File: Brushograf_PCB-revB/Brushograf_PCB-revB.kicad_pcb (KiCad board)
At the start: 2 copper layers, 200 x 60 mm, 76 parts, among them J1 Conn_01x05_Socket, J12 USB-C PD in, J13 Pendant, J2 Conn_01x05_Socket, J3 Conn_01x05_Socket, J8 SD_CARD_MICRO_AMPHENOL_114008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, SW1 ESP POWER, SW2 SW_Lever_1P2T_NKK_GW12LxH, U1 ULN2003A, U2 ULN2003A, U3 ULN2003A, U4 ESP32-DevKitC, U6 CH224K, U7 TPS54202, U8 TPS54202

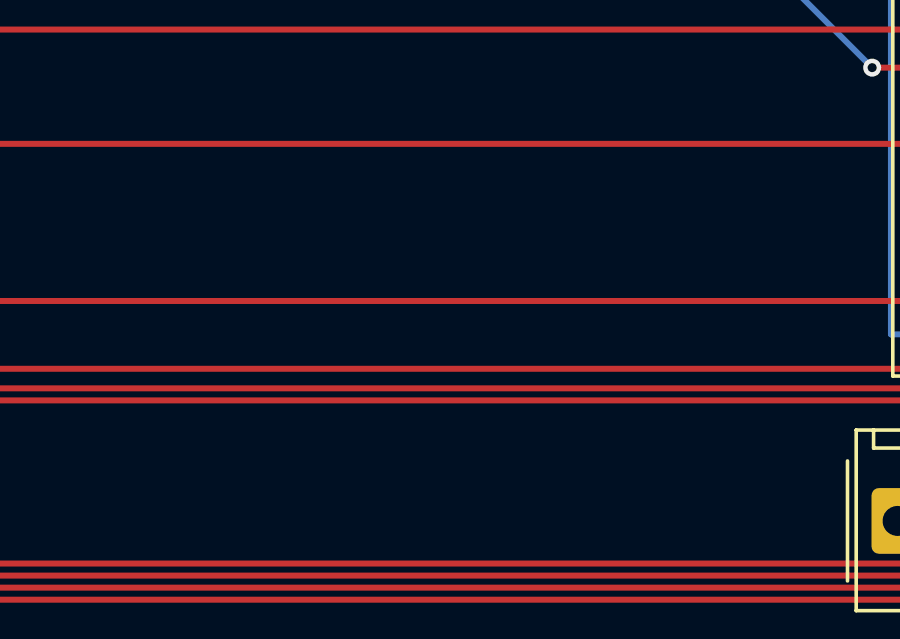
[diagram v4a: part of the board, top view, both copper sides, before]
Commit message: Move J7 to Y=50 and swap GND/PROBE pinout
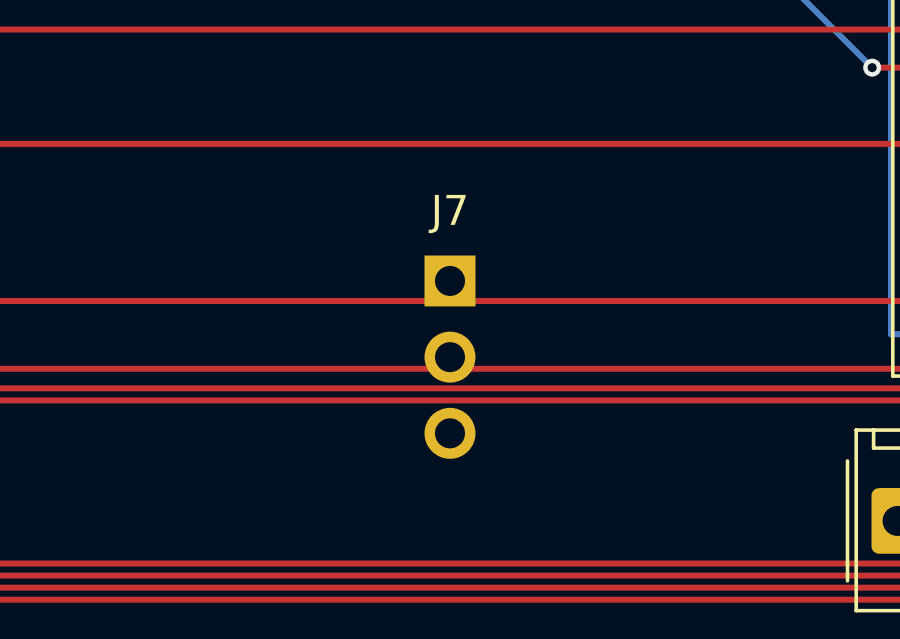
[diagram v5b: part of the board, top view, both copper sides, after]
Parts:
- added J7: Conn_01x03_Pin, Connector_PinHeader_2.54mm:PinHeader_1x03_P2.54mm_Vertical, F.Cu at (110.0, 50.0)
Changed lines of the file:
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@@
 		)
 		(embedded_fonts no)
-		(model "${KICAD8_3DMODEL_DIR}/LED_THT.3dshapes/LED_D1.8mm_W3.3mm_H2.4mm.wrl"
+		(model "${KICAD10_3DMODEL_DIR}/LED_THT.3dshapes/LED_D1.8mm_W3.3mm_H2.4mm.step"
 			(offset
 				(xyz 0 0 0)
@@
 		)
 		(embedded_fonts no)
-		(model "${KICAD8_3DMODEL_DIR}/LED_THT.3dshapes/LED_D1.8mm_W3.3mm_H2.4mm.wrl"
+		(model "${KICAD10_3DMODEL_DIR}/LED_THT.3dshapes/LED_D1.8mm_W3.3mm_H2.4mm.step"
 			(offset
 				(xyz 0 0 0)
@@
 		)
 		(embedded_fonts no)
-		(model "${KICAD8_3DMODEL_DIR}/Connector_Molex.3dshapes/Molex_KK-254_AE-6410-05A_1x05_P2.54mm_Vertical.wrl"
+		(model "${KICAD10_3DMODEL_DIR}/Connector_Molex.3dshapes/Molex_KK-254_AE-6410-05A_1x05_P2.54mm_Vertical.step"
 			(offset
 				(xyz 0 0 0)
@@
 		)
 		(embedded_fonts no)
-		(model "${KICAD8_3DMODEL_DIR}/LED_THT.3dshapes/LED_D1.8mm_W3.3mm_H2.4mm.wrl"
+		(model "${KICAD10_3DMODEL_DIR}/LED_THT.3dshapes/LED_D1.8mm_W3.3mm_H2.4mm.step"
 			(offset
 				(xyz 0 0 0)
@@
 		)
 		(embedded_fonts no)
-		(model "${KICAD8_3DMODEL_DIR}/Package_DIP.3dshapes/DIP-16_W7.62mm_Socket.wrl"
+		(model "${KICAD10_3DMODEL_DIR}/Package_DIP.3dshapes/DIP-16_W7.62mm_Socket.step"
 			(offset
 				(xyz 0 0 0)
@@
 		)
 		(embedded_fonts no)
-		(model "${KICAD8_3DMODEL_DIR}/LED_THT.3dshapes/LED_D1.8mm_W3.3mm_H2.4mm.wrl"
+		(model "${KICAD10_3DMODEL_DIR}/LED_THT.3dshapes/LED_D1.8mm_W3.3mm_H2.4mm.step"
 			(offset
 				(xyz 0 0 0)
@@
 		)
 		(embedded_fonts no)
-		(model "${KICAD8_3DMODEL_DIR}/LED_THT.3dshapes/LED_D1.8mm_W3.3mm_H2.4mm.wrl"
+		(model "${KICAD10_3DMODEL_DIR}/LED_THT.3dshapes/LED_D1.8mm_W3.3mm_H2.4mm.step"
 			(offset
 				(xyz 0 0 0)
@@
 		)
 		(embedded_fonts no)
-		(model "${KICAD8_3DMODEL_DIR}/LED_THT.3dshapes/LED_D1.8mm_W3.3mm_H2.4mm.wrl"
+		(model "${KICAD10_3DMODEL_DIR}/LED_THT.3dshapes/LED_D1.8mm_W3.3mm_H2.4mm.step"
 			(offset
 				(xyz 0 0 0)
@@
 		)
 		(embedded_fonts no)
-		(model "${KICAD8_3DMODEL_DIR}/LED_THT.3dshapes/LED_D1.8mm_W3.3mm_H2.4mm.wrl"
+		(model "${KICAD10_3DMODEL_DIR}/LED_THT.3dshapes/LED_D1.8mm_W3.3mm_H2.4mm.step"
 			(offset
 				(xyz 0 0 0)
@@
 		)
 		(embedded_fonts no)
-		(model "${KICAD8_3DMODEL_DIR}/LED_THT.3dshapes/LED_D1.8mm_W3.3mm_H2.4mm.wrl"
+		(model "${KICAD10_3DMODEL_DIR}/LED_THT.3dshapes/LED_D1.8mm_W3.3mm_H2.4mm.step"
 			(offset
 				(xyz 0 0 0)
@@
 		)
 		(embedded_fonts no)
-		(model "${KICAD8_3DMODEL_DIR}/Package_DIP.3dshapes/DIP-16_W7.62mm_Socket.wrl"
+		(model "${KICAD10_3DMODEL_DIR}/Package_DIP.3dshapes/DIP-16_W7.62mm_Socket.step"
 			(offset
 				(xyz 0 0 0)
@@
 		)
 		(embedded_fonts no)
-		(model "${KICAD8_3DMODEL_DIR}/LED_THT.3dshapes/LED_D1.8mm_W3.3mm_H2.4mm.wrl"
+		(model "${KICAD10_3DMODEL_DIR}/LED_THT.3dshapes/LED_D1.8mm_W3.3mm_H2.4mm.step"
 			(offset
 				(xyz 0 0 0)
@@
 		)
 		(embedded_fonts no)
-		(model "${KICAD8_3DMODEL_DIR}/Connector_Molex.3dshapes/Molex_KK-254_AE-6410-05A_1x05_P2.54mm_Vertical.wrl"
+		(model "${KICAD10_3DMODEL_DIR}/Connector_Molex.3dshapes/Molex_KK-254_AE-6410-05A_1x05_P2.54mm_Vertical.step"
 			(offset
 				(xyz 0 0 0)
@@
 		)
 		(embedded_fonts no)
-		(model "${KICAD8_3DMODEL_DIR}/LED_THT.3dshapes/LED_D1.8mm_W3.3mm_H2.4mm.wrl"
+		(model "${KICAD10_3DMODEL_DIR}/LED_THT.3dshapes/LED_D1.8mm_W3.3mm_H2.4mm.step"
 			(offset
 				(xyz 0 0 0)
@@
 		)
 		(embedded_fonts no)
-		(model "${KICAD8_3DMODEL_DIR}/Connector_Molex.3dshapes/Molex_KK-254_AE-6410-05A_1x05_P2.54mm_Vertical.wrl"
+		(model "${KICAD10_3DMODEL_DIR}/Connector_Molex.3dshapes/Molex_KK-254_AE-6410-05A_1x05_P2.54mm_Vertical.step"
 			(offset
 				(xyz 0 0 0)
@@
 		)
 		(embedded_fonts no)
-		(model "${KICAD8_3DMODEL_DIR}/LED_THT.3dshapes/LED_D1.8mm_W3.3mm_H2.4mm.wrl"
+		(model "${KICAD10_3DMODEL_DIR}/LED_THT.3dshapes/LED_D1.8mm_W3.3mm_H2.4mm.step"
 			(offset
 				(xyz 0 0 0)
@@
 		)
 		(embedded_fonts no)
-		(model "${KICAD8_3DMODEL_DIR}/Package_DIP.3dshapes/DIP-16_W7.62mm_Socket.wrl"
+		(model "${KICAD10_3DMODEL_DIR}/Package_DIP.3dshapes/DIP-16_W7.62mm_Socket.step"
 			(offset
 				(xyz 0 0 0)
@@
 		)
 		(embedded_fonts no)
-		(model "${KICAD8_3DMODEL_DIR}/LED_THT.3dshapes/LED_D1.8mm_W3.3mm_H2.4mm.wrl"
+		(model "${KICAD10_3DMODEL_DIR}/LED_THT.3dshapes/LED_D1.8mm_W3.3mm_H2.4mm.step"
 			(offset
 				(xyz 0 0 0)
@@
 		)
 		(embedded_fonts no)
-		(model "${KISYS3DMOD}/Resistor_SMD.3dshapes/R_1206_3216Metric.wrl"
+		(model "${KICAD10_3DMODEL_DIR}/Resistor_SMD.3dshapes/R_1206_3216Metric.step"
 			(offset
 				(xyz 0 0 0)
@@
 		)
 		(embedded_fonts no)
-		(model "${KISYS3DMOD}/Resistor_SMD.3dshapes/R_1206_3216Metric.wrl"
+		(model "${KICAD10_3DMODEL_DIR}/Resistor_SMD.3dshapes/R_1206_3216Metric.step"
 			(offset
 				(xyz 0 0 0)
@@
 		)
 		(embedded_fonts no)
-		(model "${KISYS3DMOD}/Resistor_SMD.3dshapes/R_1206_3216Metric.wrl"
+		(model "${KICAD10_3DMODEL_DIR}/Resistor_SMD.3dshapes/R_1206_3216Metric.step"
 			(offset
 				(xyz 0 0 0)
@@
 		)
 		(embedded_fonts no)
-		(model "${KISYS3DMOD}/Resistor_SMD.3dshapes/R_1206_3216Metric.wrl"
+		(model "${KICAD10_3DMODEL_DIR}/Resistor_SMD.3dshapes/R_1206_3216Metric.step"
 			(offset
 				(xyz 0 0 0)
@@
 		)
 		(embedded_fonts no)
-		(model "${KICAD6_3DMODEL_DIR}/Capacitor_SMD.3dshapes/C_1206_3216Metric.wrl"
+		(model "${KICAD10_3DMODEL_DIR}/Capacitor_SMD.3dshapes/C_1206_3216Metric.step"
 			(offset
 				(xyz 0 0 0)
@@
 		)
 		(embedded_fonts no)
-		(model "${KICAD6_3DMODEL_DIR}/Capacitor_SMD.3dshapes/C_1206_3216Metric.wrl"
+		(model "${KICAD10_3DMODEL_DIR}/Capacitor_SMD.3dshapes/C_1206_3216Metric.step"
 			(offset
 				(xyz 0 0 0)
@@
 		)
 		(embedded_fonts no)
-		(model "${KISYS3DMOD}/Resistor_SMD.3dshapes/R_1206_3216Metric.wrl"
+		(model "${KICAD10_3DMODEL_DIR}/Resistor_SMD.3dshapes/R_1206_3216Metric.step"
 			(offset
 				(xyz 0 0 0)
@@
 		)
 		(embedded_fonts no)
-		(model "${KISYS3DMOD}/Resistor_SMD.3dshapes/R_1206_3216Metric.wrl"
+		(model "${KICAD10_3DMODEL_DIR}/Resistor_SMD.3dshapes/R_1206_3216Metric.step"
 			(offset
 				(xyz 0 0 0)
@@
 		)
 		(embedded_fonts no)
-		(model "${KISYS3DMOD}/Resistor_SMD.3dshapes/R_1206_3216Metric.wrl"
+		(model "${KICAD10_3DMODEL_DIR}/Resistor_SMD.3dshapes/R_1206_3216Metric.step"
 			(offset
 				(xyz 0 0 0)
@@
 		)
 		(embedded_fonts no)
-		(model "${KISYS3DMOD}/Resistor_SMD.3dshapes/R_1206_3216Metric.wrl"
+		(model "${KICAD10_3DMODEL_DIR}/Resistor_SMD.3dshapes/R_1206_3216Metric.step"
 			(offset
 				(xyz 0 0 0)
@@
 		)
 		(embedded_fonts no)
-		(model "${KISYS3DMOD}/Resistor_SMD.3dshapes/R_1206_3216Metric.wrl"
+		(model "${KICAD10_3DMODEL_DIR}/Resistor_SMD.3dshapes/R_1206_3216Metric.step"
 			(offset
 				(xyz 0 0 0)
@@
 		)
 		(embedded_fonts no)
-		(model "${KISYS3DMOD}/Resistor_SMD.3dshapes/R_1206_3216Metric.wrl"
+		(model "${KICAD10_3DMODEL_DIR}/Resistor_SMD.3dshapes/R_1206_3216Metric.step"
 			(offset
 				(xyz 0 0 0)
@@
 		)
 		(embedded_fonts no)
-		(model "${KISYS3DMOD}/Resistor_SMD.3dshapes/R_1206_3216Metric.wrl"
+		(model "${KICAD10_3DMODEL_DIR}/Resistor_SMD.3dshapes/R_1206_3216Metric.step"
 			(offset
 				(xyz 0 0 0)
@@
 		)
 		(embedded_fonts no)
-		(model "${KISYS3DMOD}/Resistor_SMD.3dshapes/R_1206_3216Metric.wrl"
+		(model "${KICAD10_3DMODEL_DIR}/Resistor_SMD.3dshapes/R_1206_3216Metric.step"
 			(offset
 				(xyz 0 0 0)
@@
 		)
 		(embedded_fonts no)
-		(model "${KICAD6_3DMODEL_DIR}/Capacitor_SMD.3dshapes/C_1206_3216Metric.wrl"
+		(model "${KICAD10_3DMODEL_DIR}/Capacitor_SMD.3dshapes/C_1206_3216Metric.step"
 			(offset
 				(xyz 0 0 0)
@@
 	)
 	(embedded_fonts no)
+	(footprint "Connector_PinHeader_2.54mm:PinHeader_1x03_P2.54mm_Vertical"
+		(layer "F.Cu")
+		(at 110 50)
+		(property "Reference" "J7"
+			(at 0 -2.33 0)
+			(layer "F.SilkS")
+			(effects
+				(font
+					(size 1 1)
+					(thickness 0.15)
+				)
+			)
+		)
+		(property "Value" "Conn_01x03_Pin"
+			(at 0 7.41 0)
+			(layer "F.Fab")
+			(effects
+				(font
+					(size 1 1)
+					(thickness 0.15)
+				)
+			)
+		)
+		(pad "1" thru_hole rect
+			(at 0 0)
+			(size 1.7 1.7)
+			(drill 1)
+			(layers "*.Cu" "*.Mask")
+			(remove_unused_layers no)
+			(net "3.3V")
+		)
+		(pad "2" thru_hole oval
+			(at 0 2.54)
+			(size 1.7 1.7)
+			(drill 1)
+			(layers "*.Cu" "*.Mask")
+			(remove_unused_layers no)
+			(net "GND")
+		)
+		(pad "3" thru_hole oval
+			(at 0 5.08)
+			(size 1.7 1.7)
+			(drill 1)
+			(layers "*.Cu" "*.Mask")
+			(remove_unused_layers no)
+			(net "PROBE")
+		)
+	)
 )

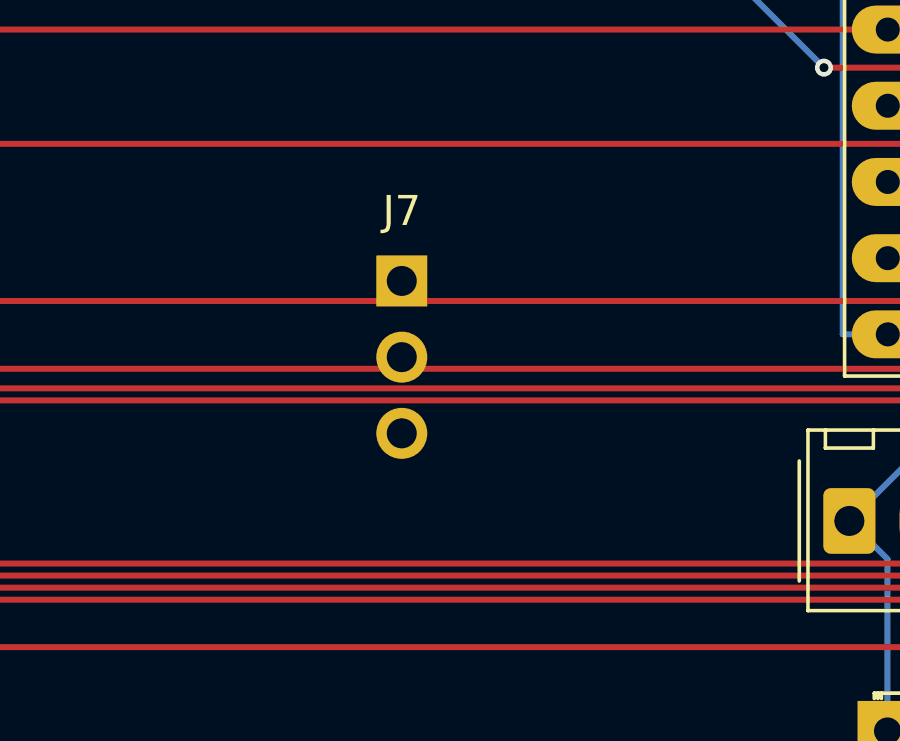
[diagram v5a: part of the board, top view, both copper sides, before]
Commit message: Change J7 to horizontal header at Y=58 and rotate 90 deg
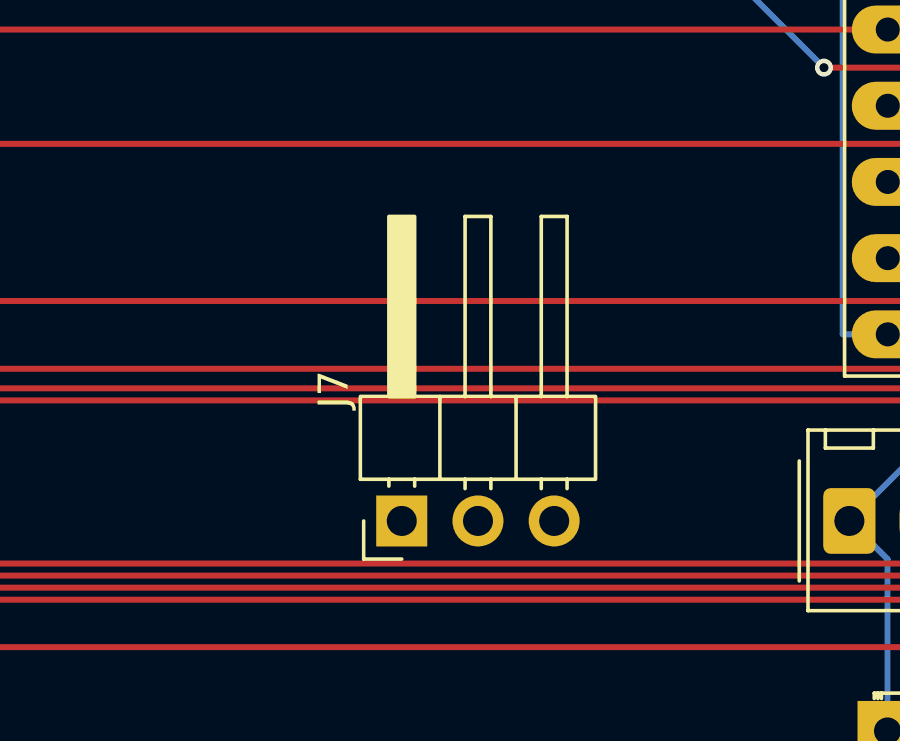
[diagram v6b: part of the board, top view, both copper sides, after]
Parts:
- J7: value Conn_01x03_Pin -> PinHeader_1x03_P2.54mm_Horizontal; footprint Connector_PinHeader_2.54mm:PinHeader_1x03_P2.54mm_Vertical -> PinHeader_1x03_P2.54mm_Horizontal
- moved J7 8.00 mm to (110.0, 58.0), turned to 90 degrees

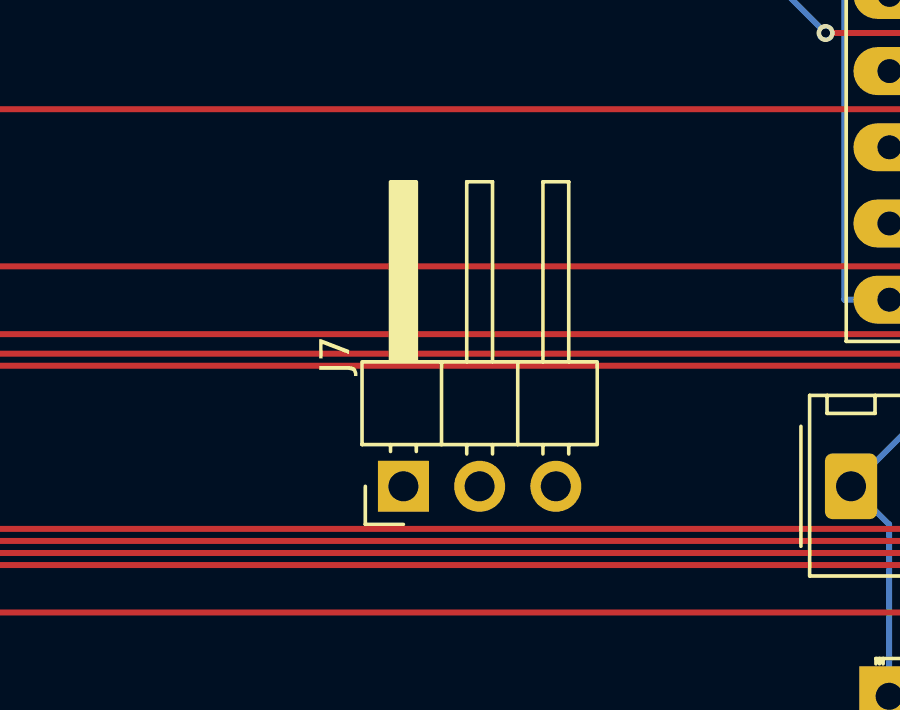
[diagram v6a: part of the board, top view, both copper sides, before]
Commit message: Change J7 to Vertical header
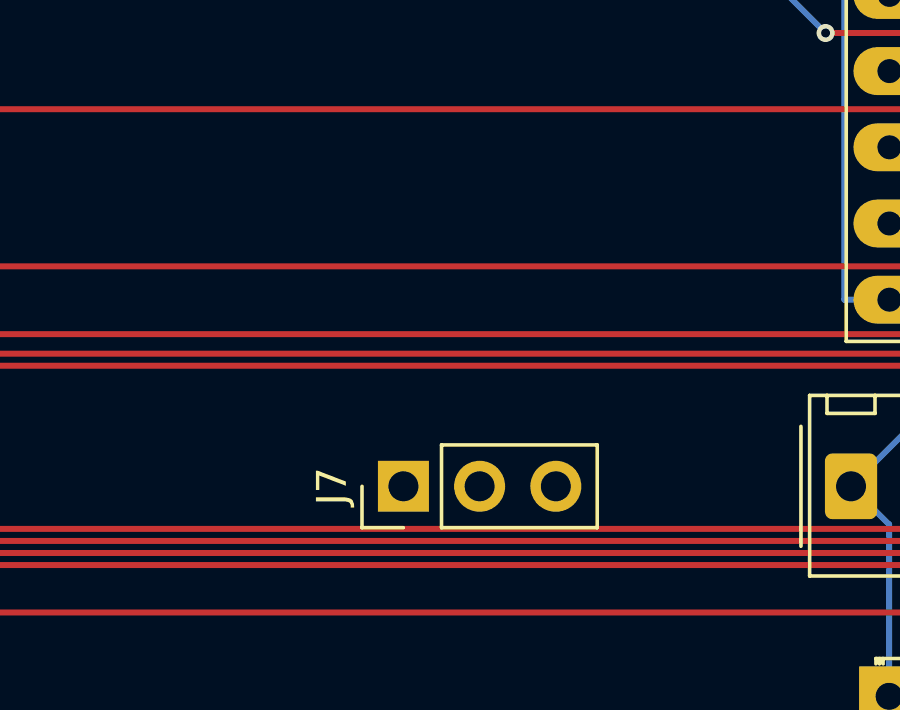
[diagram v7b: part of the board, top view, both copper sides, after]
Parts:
- J7: value PinHeader_1x03_P2.54mm_Horizontal -> PinHeader_1x03_P2.54mm_Vertical; footprint PinHeader_1x03_P2.54mm_Horizontal -> PinHeader_1x03_P2.54mm_Vertical

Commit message: Move USB-C to Y=15.84 and Switches to Y=22. Add LEDs with Brushograph footprints
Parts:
- added D_SW1: LED, 009_Brushograph:LED_D1.8mm_Brushograf, F.Cu at (35.0, 32.0)
- added D_SW2: LED, 009_Brushograph:LED_D1.8mm_Brushograf, F.Cu at (48.0, 32.0)
- added D_USB: LED, 009_Brushograph:LED_D1.8mm_Brushograf, F.Cu at (20.2, 30.0)
- added R_SW1: 10k, Potentiometer_THT:Potentiometer_Bourns_3296W_Vertical, F.Cu at (35.0, 28.0)
- added R_SW2: 10k, Potentiometer_THT:Potentiometer_Bourns_3296W_Vertical, F.Cu at (48.0, 28.0)
- added R_USB: 10k, Potentiometer_THT:Potentiometer_Bourns_3296W_Vertical, F.Cu at (20.2, 26.0)
- moved J12 4.36 mm to (20.2, 15.8)
- moved SW1 4.00 mm to (35.0, 22.0)
- moved SW2 4.00 mm to (48.0, 22.0)
